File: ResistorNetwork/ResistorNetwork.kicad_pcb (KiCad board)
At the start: 2 copper layers, 94 x 45.7 mm, 12 parts

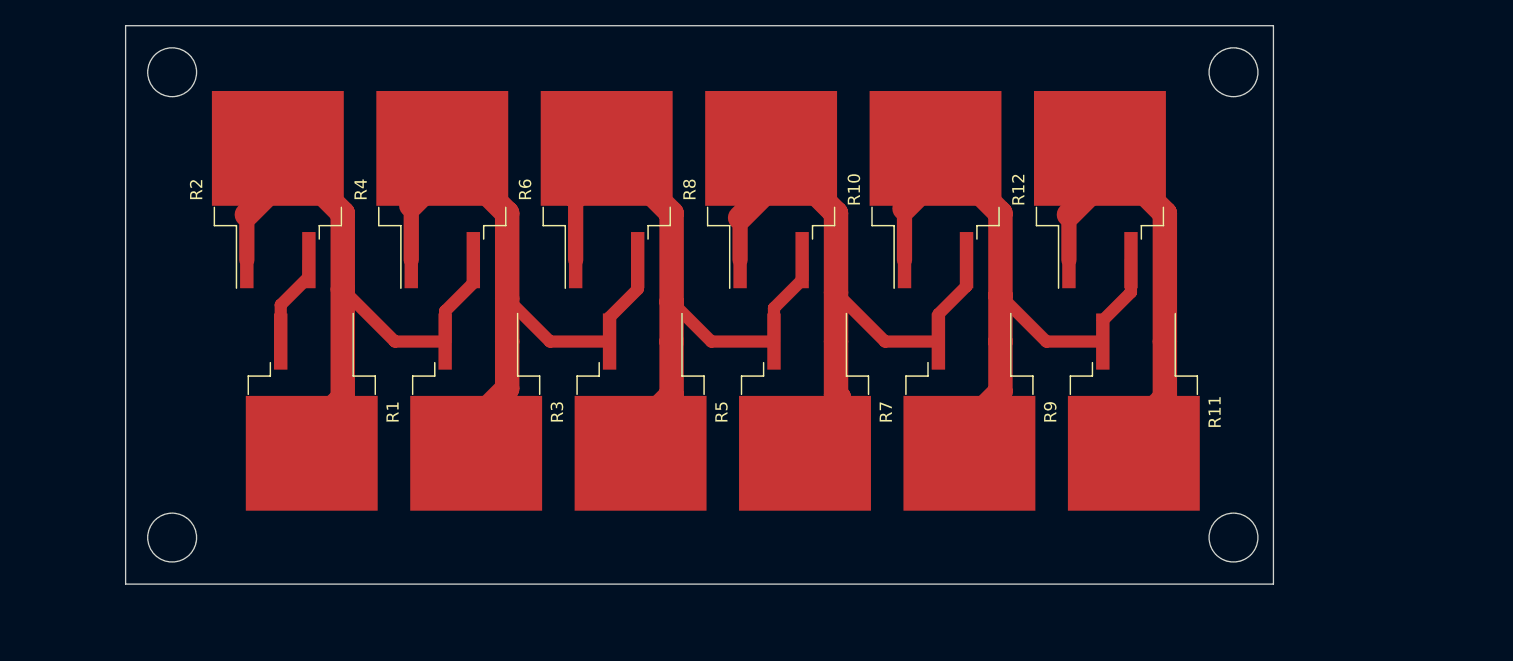
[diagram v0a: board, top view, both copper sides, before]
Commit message: resistor network layout done
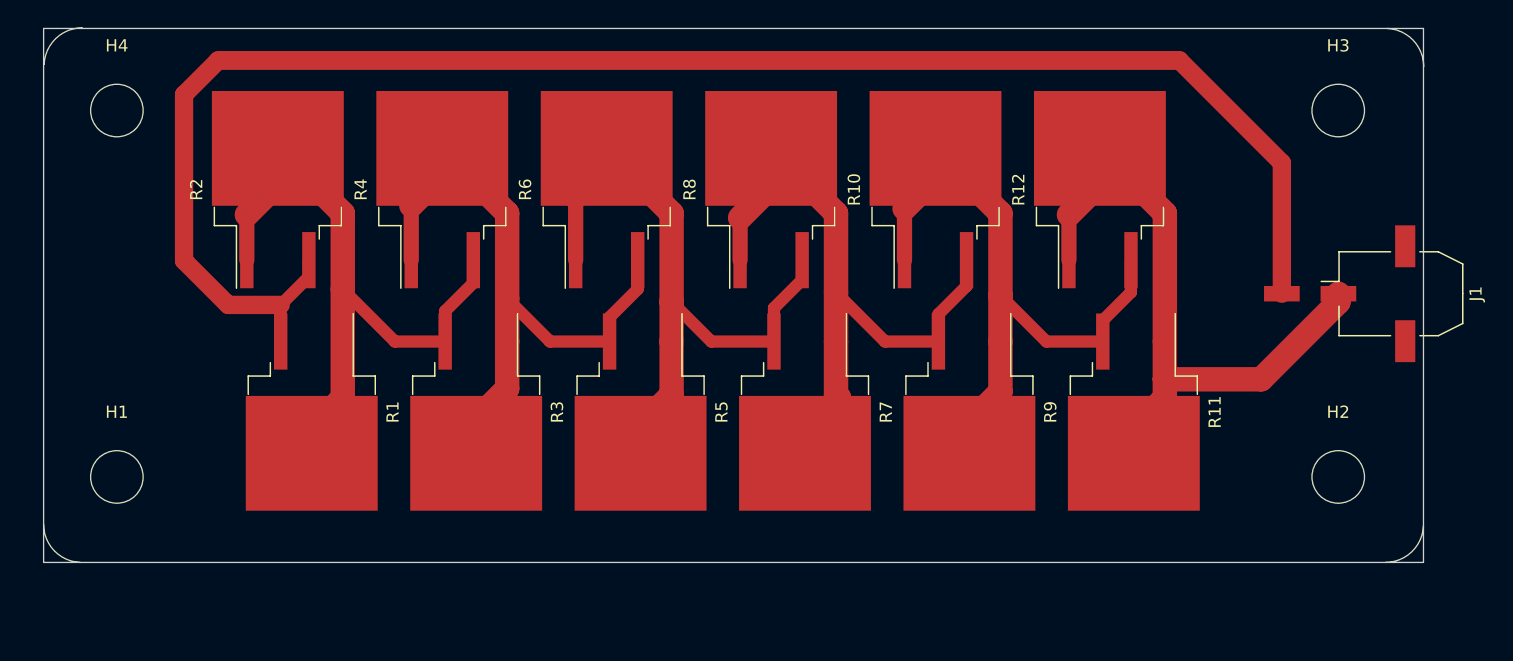
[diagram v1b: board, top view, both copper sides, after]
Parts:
- added H1: MountingHole, MountingHole:MountingHole_4.3mm_M4, F.Cu at (30.0, 65.0)
- added H2: MountingHole, MountingHole:MountingHole_4.3mm_M4, F.Cu at (130.0, 65.0)
- added H3: MountingHole, MountingHole:MountingHole_4.3mm_M4, F.Cu at (130.0, 35.0)
- added H4: MountingHole, MountingHole:MountingHole_4.3mm_M4, F.Cu at (30.0, 35.0)
- added J1: Conn_01x02_Female, Connector_Molex:Molex_Micro-Fit_3.0_43045-0210_2x01-1MP_P3.00mm_Horizontal, F.Cu at (127.7, 50.0)
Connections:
- net /Network_in renamed /Network_In
- net /Network_out renamed /Network_Out
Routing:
- net /Network_In: track 7.62 -> 135.9 mm
- net /Network_Out: track 38.4 -> 55.9 mm
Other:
- board size 94 x 45.7 mm -> 113 x 43.8 mm

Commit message: added new relay and TSMP resistors
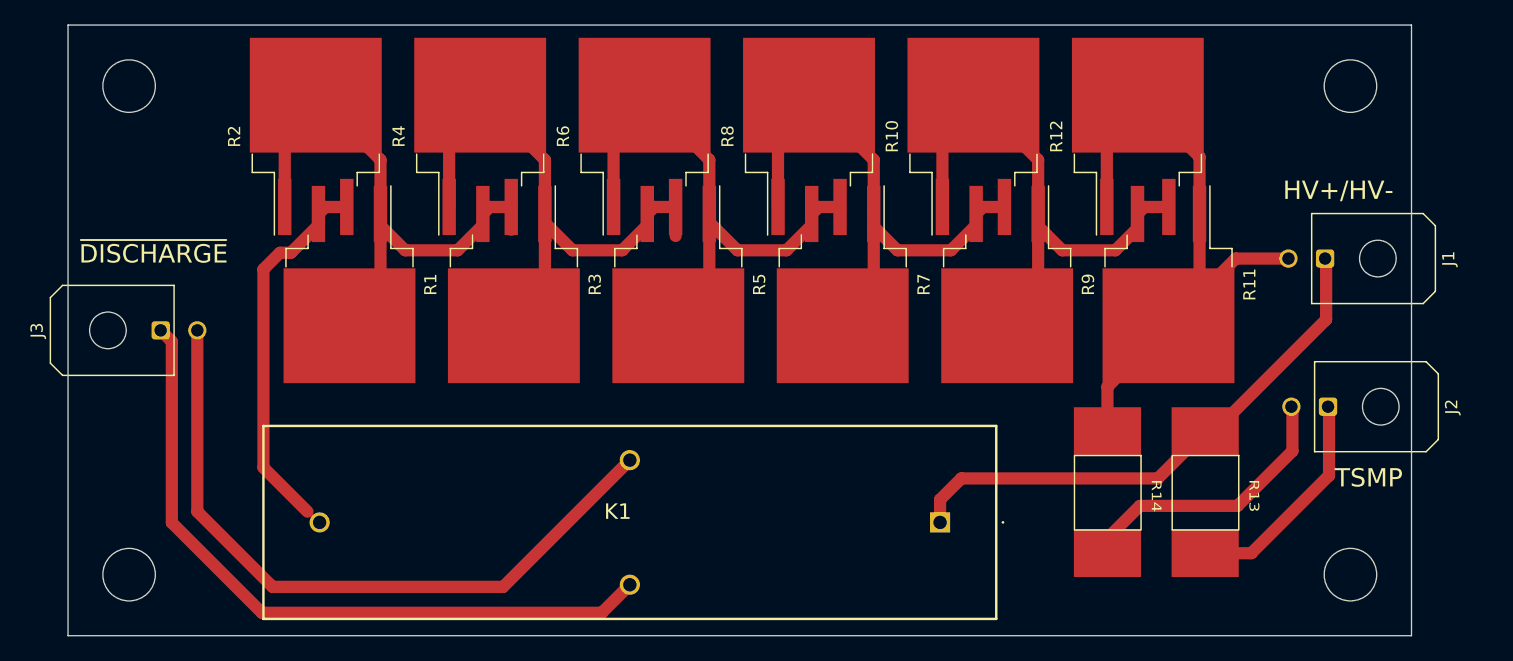
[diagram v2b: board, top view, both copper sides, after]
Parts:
- added J2: Conn_01x02_Female, Connector_Molex:Molex_Micro-Fit_3.0_43045-0200_2x01_P3.00mm_Horizontal, F.Cu at (129.2, 59.2)
- added J3: Conn_01x02_Female, Connector_Molex:Molex_Micro-Fit_3.0_43045-0200_2x01_P3.00mm_Horizontal, F.Cu at (33.6, 53.0)
- added K1: DBR72410, Reed Relay:DBT70510U, F.Cu at (97.4, 68.7)
- added R13: R, Resistor_SMD:3550 Resistor TE, F.Cu at (116.4, 59.3)
- added R14: R, Resistor_SMD:3550 Resistor TE, F.Cu at (108.4, 59.3)
- J1: footprint Connector_Molex:Molex_Micro-Fit_3.0_43045-0210_2x01-1MP_P3.00mm_Horizontal -> Connector_Molex:Molex_Micro-Fit_3.0_43045-0200_2x01_P3.00mm_Horizontal
- R1, R10, R11, R12, R2, R3, R4, R5, R6, R7, R8, R9: value 250R -> 470R
- moved R7 10.9 mm to (89.4, 49.2)
- moved R1 10.9 mm to (49.0, 49.2)
- moved R3 10.9 mm to (62.5, 49.2)
- moved R5 10.9 mm to (76.0, 49.2)
- moved R9 10.9 mm to (102.9, 49.2)
- moved R11 10.8 mm to (116.1, 49.2)
- moved H1 8.06 mm to (31.0, 73.0)
- moved H2 8.06 mm to (131.0, 73.0)
- moved R12 5.35 mm to (113.6, 37.1)
- moved R6 5.35 mm to (73.2, 37.1)
- moved R8 5.35 mm to (86.7, 37.1)
- moved R2 5.35 mm to (46.3, 37.1)
- moved R4 5.35 mm to (59.7, 37.1)
- moved R10 5.35 mm to (100.1, 37.1)
- moved J1 3.13 mm to (128.9, 47.1)
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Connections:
- J1 pad 1: /Network_Out -> /HV+
- J1 pad 2: /Network_In -> /HV-
- R1 pad 2: /Network_In -> Net-(R1-Pad2)
- R11 pad 1: /Network_Out -> /HV-
- R12 pad 1: /Network_Out -> /HV-
- R2 pad 2: /Network_In -> Net-(R1-Pad2)
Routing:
- net /Network_In: track 135.9 -> 0.00 mm
- net /~{Discharge}: track 0.00 -> 57.6 mm
- net GND: track 0.00 -> 57.1 mm
- net /Network_Out: track 55.9 -> 0.00 mm
- net /HV-: track 0.00 -> 55.0 mm
- net /HV+: track 0.00 -> 44.6 mm
- net Net-(R1-Pad2): track 0.00 -> 32.2 mm
- net /HV-_TSMP: track 0.00 -> 22.9 mm
- net /HV+_TSMP: track 0.00 -> 18.8 mm
- net Net-(R10-Pad1): track 56.0 -> 47.0 mm
- net Net-(R5-Pad1): track 55.8 -> 48.3 mm
- net Net-(R1-Pad1): track 56.2 -> 48.7 mm
- net Net-(R3-Pad1): track 55.9 -> 49.1 mm
- net Net-(R10-Pad2): track 59.2 -> 52.9 mm
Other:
- board size 113 x 43.8 mm -> 110 x 50 mm
- board text added: "HV+/HV-"
- board text added: "TSMP"
- board text added: "~{DISCHARGE}"
